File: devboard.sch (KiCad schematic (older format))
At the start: 1 part

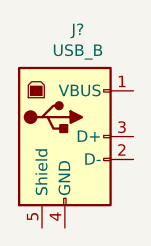
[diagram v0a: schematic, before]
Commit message: changed names
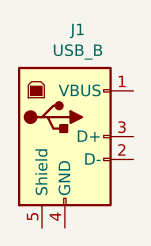
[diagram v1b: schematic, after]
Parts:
- gave numbers to parts that had none: 1
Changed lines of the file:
@@
 encoding utf-8
 Sheet 1 1
-Title "AVR devboard"
-Date "2021-08-16"
-Rev "1.0"
-Comp "Mateusz Wasik Michał Penkal"
+Title "Devboard"
+Date ""
+Rev ""
+Comp ""
 Comment1 ""
 Comment2 ""
@@
 $EndDescr
 $Comp
-L Connector:USB_B J?
+L Connector:USB_B J1
 U 1 1 611B35D4
 P 2500 2950
-F 0 "J?" H 2557 3417 50  0000 C CNN
+F 0 "J1" H 2557 3417 50  0000 C CNN
 F 1 "USB_B" H 2557 3326 50  0000 C CNN
 F 2 "" H 2650 2900 50  0001 C CNN

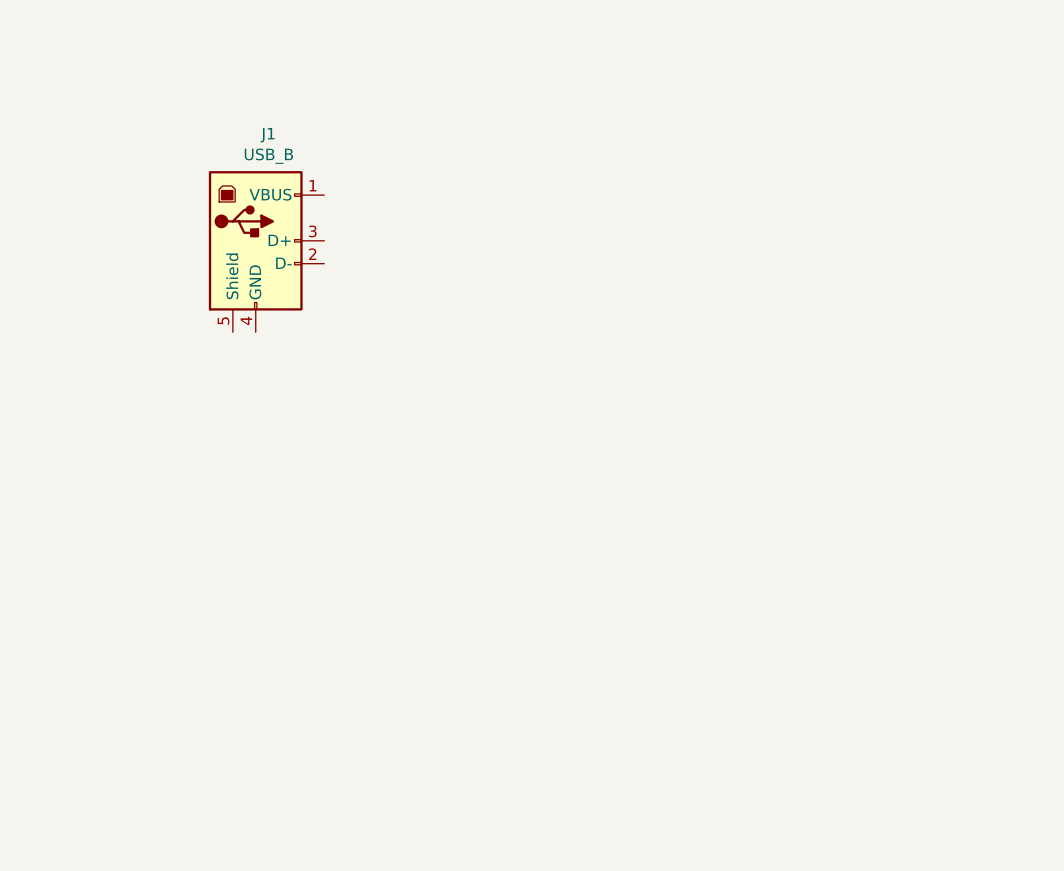
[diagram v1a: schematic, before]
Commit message: Power from USB socket
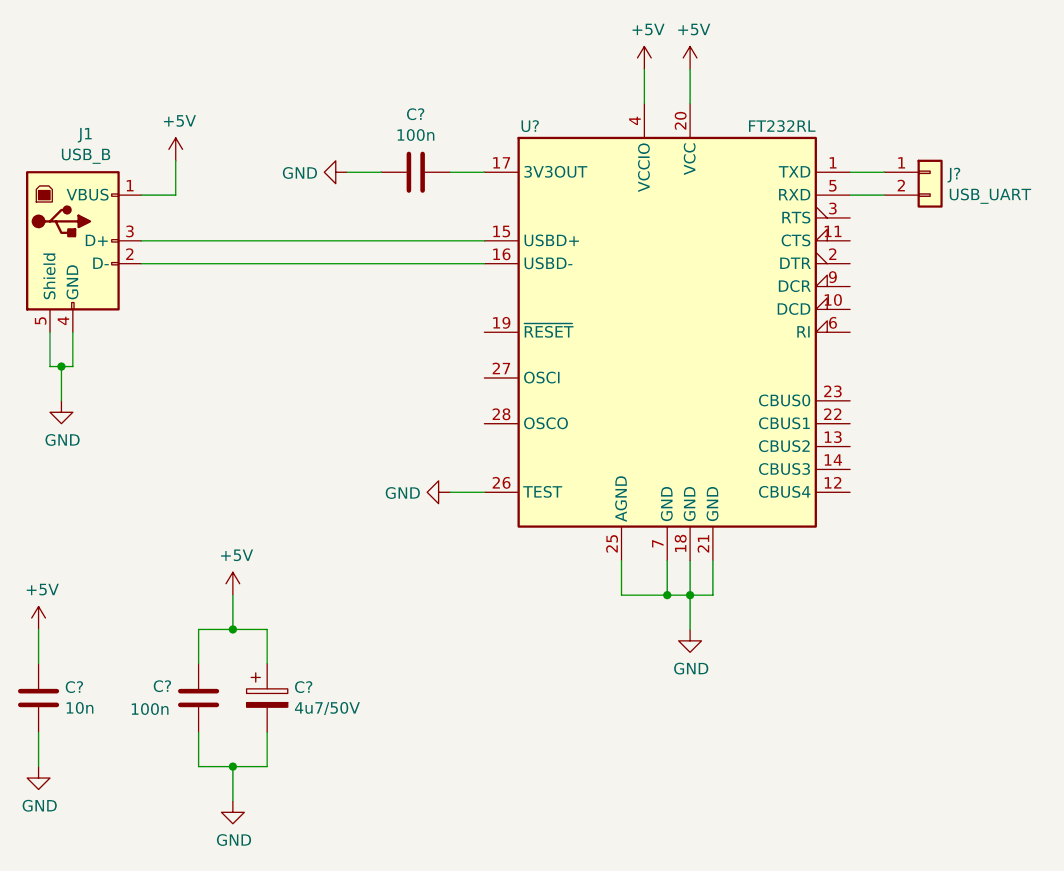
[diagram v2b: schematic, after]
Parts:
- added C? (x2): 100n, symbol Device:C
- added C?: 10n, symbol Device:C
- added C?: 4u7/50V, symbol Device:CP
- added J?: USB_UART, symbol Connector_Generic:Conn_01x02
- added U?: FT232RL, Package_SO:SSOP-28_5.3x10.2mm_P0.65mm, symbol Interface_USB:FT232RL
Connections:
- net +5V: now reaches J1.1 (VBUS)
- net +5V: now also C?.1, C?.2, C?.2, U?.20 (VCC), U?.4 (VCCIO)
- net at J1.2 (D-): now also U?.16 (USBD-)
- net at J1.3 (D+): now also U?.15 (USBD+)
- net GND: now reaches J1.4 (GND)
- net GND: now also J1.5 (Shield), C?.1, C?.1, C?.2, C?.2, U?.18 (GND), U?.21 (GND), U?.25 (AGND), U?.26 (TEST), U?.7 (GND)
- new net: J?.1 (Pin_1), U?.1 (TXD)
- new net: C?.1, U?.17 (3V3OUT)
- new net: J?.2 (Pin_2), U?.5 (RXD)
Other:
- moved on the sheet: J1

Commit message: power dokończony essa
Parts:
- added C?: 10u, symbol Device:CP
- added J?: USB_Control, symbol Connector_Generic:Conn_01x06
- added J?: USB_CBUS, symbol Connector_Generic:Conn_01x06
- added U?: ATmega8A, Package_DIP:DIP-28_W7.62mm, symbol MCU_Microchip_ATmega:ATmega8A-PU
- added Y?: 12M, symbol Device:Crystal_Small
- C?: value 4u7/50V -> 4u7
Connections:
- net +5V: now also C?.1
- net GND: now also C?.2
- net at U?.10 (DCD): now also J?.5 (Pin_5)
- net at U?.11 (CTS): now also J?.2 (Pin_2)
- net at U?.12 (CBUS4): now also J?.5 (Pin_5)
- net at U?.13 (CBUS2): now also J?.3 (Pin_3)
- net at U?.14 (CBUS3): now also J?.4 (Pin_4)
- net at U?.19 (~RESET~): now also J?.6 (Pin_6)
- net at U?.2 (DTR): now also J?.3 (Pin_3)
- net at U?.22 (CBUS1): now also J?.2 (Pin_2)
- net at U?.23 (CBUS0): now also J?.1 (Pin_1)
- net at U?.27 (OSCI): now also Y?.1
- net at U?.28 (OSCO): now also Y?.2
- net at U?.3 (RTS): now also J?.1 (Pin_1)
- net at U?.6 (RI): now also J?.6 (Pin_6)
- net at U?.9 (DCR): now also J?.4 (Pin_4)
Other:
- note added: "USB + Power"
- moved on the sheet: C?, J1, J?, U?

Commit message: MCU + CLK
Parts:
- added C? (x3): 100n, symbol Device:C
- added C?: 10n, symbol Device:C
- added C? (x2): 22p, symbol Device:C
- added JP?: Reset, symbol Device:Jumper_NC_Small
- added JP?: ARef, symbol Device:Jumper_NC_Small
- added JP?: XTAL1, symbol Device:Jumper_NC_Small
- added JP?: XTAL2, symbol Device:Jumper_NC_Small
- added L?: 10u, symbol Device:L
- added R?: 10k, symbol Device:R
- added U?: MCP1525, Package_TO_SOT_THT:TO-92_Inline, symbol Reference_Voltage:MCP1525-TO
- added Y?: 16M, symbol Device:Crystal_Small
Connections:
- net +5V: now also U?.7 (VCC), C?.2, C?.2, L?.1, R?.2, U?.3 (Vin)
- net GND: now also U?.22 (AGND), U?.8 (GND), C?.1, C?.1, C?.1, C?.1, C?.2, C?.2, U?.1 (Vss)
- net Reset: now reaches U?.1 (PC6/~RESET)
- net Reset: now also JP?.2
- net XTAL2: now reaches U?.10 (PB7/XTAL2)
- net XTAL2: now also JP?.2
- net at U?.20 (AVCC): now also C?.2, L?.2
- net A_Ref: now reaches U?.21 (AREF)
- net A_Ref: now also JP?.2
- net XTAL1: now reaches U?.9 (PB6/XTAL1)
- net XTAL1: now also JP?.2
- new net: JP?.1, R?.1
- new net: C?.2, JP?.1, U?.2 (Vout)
- new net: C?.1, JP?.1, Y?.1
- new net: C?.1, JP?.1, Y?.2

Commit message: Programming, port goldpins, a bit of cleanup
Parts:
- added J?: PORTB, symbol Connector_Generic:Conn_01x08
- added J?: PORTC, symbol Connector_Generic:Conn_01x07
- added J?: PORTD, symbol Connector_Generic:Conn_01x08
- added J?: AVR-ISP, symbol Connector:AVR-ISP-10
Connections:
- net +5V: now also J?.2 (VCC)
- net GND: now also J?.10 (GND), J?.4 (GND), J?.6 (GND), J?.8 (GND)
- net PD5: now reaches U?.11 (PD5)
- net PD5: now also J?.6 (Pin_6)
- net PD6: now reaches U?.12 (PD6)
- net PD6: now also J?.7 (Pin_7)
- net PD7: now reaches U?.13 (PD7)
- net PD7: now also J?.8 (Pin_8)
- net PB0: now reaches U?.14 (PB0)
- net PB0: now also J?.1 (Pin_1)
- net PB1: now reaches U?.15 (PB1)
- net PB1: now also J?.2 (Pin_2)
- net PB2: now reaches U?.16 (PB2)
- net PB2: now also J?.3 (Pin_3)
- net MOSI: now reaches U?.17 (PB3)
- net MOSI: now also J?.1 (MOSI), J?.4 (Pin_4)
- net MISO: now reaches U?.18 (PB4)
- net MISO: now also J?.5 (Pin_5), J?.9 (MISO)
- net PB5: now reaches U?.19 (PB5)
- net PB5: now also J?.6 (Pin_6), J?.7 (SCK)
- net PD0: now reaches U?.2 (PD0)
- net PD0: now also J?.1 (Pin_1)
- net PC0: now reaches U?.23 (PC0)
- net PC0: now also J?.1 (Pin_1)
- net PC1: now reaches U?.24 (PC1)
- net PC1: now also J?.2 (Pin_2)
- net PC2: now reaches U?.25 (PC2)
- net PC2: now also J?.3 (Pin_3)
- net PC3: now reaches U?.26 (PC3)
- net PC3: now also J?.4 (Pin_4)
- net PC4: now reaches U?.27 (PC4)
- net PC4: now also J?.5 (Pin_5)
- net PC5: now reaches U?.28 (PC5)
- net PC5: now also J?.6 (Pin_6)
- net PD1: now reaches U?.3 (PD1)
- net PD1: now also J?.2 (Pin_2)
- net PD2: now reaches U?.4 (PD2)
- net PD2: now also J?.3 (Pin_3)
- net PD3: now reaches U?.5 (PD3)
- net PD3: now also J?.4 (Pin_4)
- net PD4: now reaches U?.6 (PD4)
- net PD4: now also J?.5 (Pin_5)
- net Reset renamed PC6
- net PC6: now also J?.5 (~RST), J?.7 (Pin_7)
- net XTAL1 renamed PB6
- net PB6: now also J?.7 (Pin_7)
- net XTAL2 renamed PB7
- net PB7: now also J?.8 (Pin_8)
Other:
- note added: "Crystal"
- note added: "Ports"
- note added: "Prog"
- note added: "Reset"
- note added: "Vref"
- moved on the sheet: C?, J1, J?, JP?, L?, R?, U?, Y?

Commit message: Added relays
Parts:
- added D? (x3): 1N4007, Diode_THT:D_DO-41_SOD81_P10.16mm_Horizontal, symbol Diode:1N4007
- added J?: Relay 1, symbol Connector_Generic:Conn_01x03
- added J?: Relay 1, symbol Connector_Generic:Conn_01x01
- added J?: Relay 2, symbol Connector_Generic:Conn_01x03
- added J?: Relay 2, symbol Connector_Generic:Conn_01x01
- added J?: Relay 3, symbol Connector_Generic:Conn_01x03
- added J?: Relay 3, symbol Connector_Generic:Conn_01x01
- added K1, K2, K?: HF3FA-012-ZTF, symbol hello-there:HF3FA-012-ZTF
- added Q? (x3): BC547, Package_TO_SOT_THT:TO-92_Inline, symbol Transistor_BJT:BC547
- added R? (x3): 1k, symbol Device:R
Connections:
- net +5V: now also D?.1 (K), D?.1 (K), D?.1 (K), K1.1, K2.1, K?.1
- net GND: now also Q?.3 (E), Q?.3 (E), Q?.3 (E)
- new net: D?.2 (A), K1.2, Q?.1 (C)
- new net: Q?.2 (B), R?.1 (x3)
- new net: J?.1 (Pin_1), K1.5
- new net: J?.2 (Pin_2), K1.4
- new net: J?.3 (Pin_3), K1.3
- new net: J?.1 (Pin_1), R?.2 (x3)
- new net: D?.2 (A), K2.2, Q?.1 (C)
- new net: J?.1 (Pin_1), K2.5
- new net: J?.2 (Pin_2), K2.4
- new net: J?.3 (Pin_3), K2.3
- new net: D?.2 (A), K?.2, Q?.1 (C)
- new net: J?.1 (Pin_1), K?.5
- new net: J?.2 (Pin_2), K?.4
- new net: J?.3 (Pin_3), K?.3
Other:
- note added: "Relays"
- moved on the sheet: C?, J1, J?, JP?, L?, R?, U?, Y?

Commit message: LED
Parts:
- added D? (x8): LED, symbol Device:LED
- added J? (x2): Conn_01x08, symbol Connector_Generic:Conn_01x08
- added R? (x8): 75, symbol Device:R
- added SW? (x8): SW_DIP_x01, symbol Switch:SW_DIP_x01
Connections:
- net GND: now also R?.2, R?.2, R?.2, R?.2, R?.2, R?.2, R?.2, R?.2, SW?.2, SW?.2, SW?.2, SW?.2, SW?.2, SW?.2, SW?.2, SW?.2
- new net: D?.1 (K), R?.1 (x8)
- new net: D?.2 (A), J?.2 (Pin_2)
- new net: D?.2 (A), J?.1 (Pin_1)
- new net: D?.2 (A), J?.3 (Pin_3)
- new net: D?.2 (A), J?.4 (Pin_4)
- new net: D?.2 (A), J?.5 (Pin_5)
- new net: D?.2 (A), J?.6 (Pin_6)
- new net: D?.2 (A), J?.7 (Pin_7)
- new net: D?.2 (A), J?.8 (Pin_8)
- new net: J?.1 (Pin_1), SW?.1
- new net: J?.2 (Pin_2), SW?.1
- new net: J?.3 (Pin_3), SW?.1
- new net: J?.4 (Pin_4), SW?.1
- new net: J?.5 (Pin_5), SW?.1
- new net: J?.6 (Pin_6), SW?.1
- new net: J?.7 (Pin_7), SW?.1
- new net: J?.8 (Pin_8), SW?.1
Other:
- note added: "LED"

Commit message: buttons in progress
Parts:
- removed J?: Conn_01x08, symbol Connector_Generic:Conn_01x08
- removed SW? (x8): SW_DIP_x01, symbol Switch:SW_DIP_x01
- added C? (x12): 100n, symbol Device:C
- added J?: DB Buttons, symbol Connector_Generic:Conn_01x04
- added J?: NDB Buttons, symbol Connector_Generic:Conn_01x04
- added R? (x12): 4k7, symbol Device:R
- added R? (x12): 330, symbol Device:R
- added SW?: B1, symbol Switch:SW_Push
- added SW?: B2, symbol Switch:SW_Push
- added SW?: B3, symbol Switch:SW_Push
- added SW?: B4, symbol Switch:SW_Push
- added SW?: B5, symbol Switch:SW_Push
- added SW?: B6, symbol Switch:SW_Push
- added SW?: B7, symbol Switch:SW_Push
- added SW?: B8, symbol Switch:SW_Push
- added SW?: Switches, symbol Switch:SW_DIP_x08
- J?: value Conn_01x08 -> LED
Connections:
- net +5V: now also R?.1, R?.1, R?.1, R?.1, R?.1, R?.1, R?.1, R?.1, R?.1, R?.1, R?.1, R?.1
- net GND: now also C?.2, C?.2, C?.2, C?.2, C?.2, C?.2, C?.2, C?.2, C?.2, C?.2, C?.2, C?.2, R?.2, R?.2, R?.2, R?.2, SW?.10, SW?.11, SW?.12, SW?.13, SW?.14, SW?.15, SW?.16, SW?.2, SW?.2, SW?.2, SW?.2, SW?.9
- new net: R?.1, SW?.2 (x4)
- new net: R?.2, SW?.1
- new net: R?.2, SW?.2
- new net: R?.2, SW?.3
- new net: R?.2, SW?.4
- new net: R?.2, SW?.5
- new net: R?.2, SW?.6
- new net: R?.2, SW?.7
- new net: R?.2, SW?.8
- new net B1: C?.1, J?.1 (Pin_1), R?.2, SW?.1
- new net B2: C?.1, J?.2 (Pin_2), R?.2, SW?.1
- new net B3: C?.1, J?.3 (Pin_3), R?.2, SW?.1
- new net B4: C?.1, J?.4 (Pin_4), R?.2, SW?.1
- new net B5: J?.1 (Pin_1), SW?.1
- new net B6: J?.2 (Pin_2), SW?.1
- new net B7: J?.3 (Pin_3), SW?.1
- new net B8: J?.4 (Pin_4), SW?.1
- new net S1: C?.1, R?.1, R?.2
- new net S2: C?.1, R?.1, R?.2
- new net S3: C?.1, R?.1, R?.2
- new net S4: C?.1, R?.1, R?.2
- new net S5: C?.1, R?.1, R?.2
- new net S6: C?.1, R?.1, R?.2
- new net S7: C?.1, R?.1, R?.2
- new net S8: C?.1, R?.1, R?.2
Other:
- note added: "CPU"
- note added: "Debounced buttons"
- note added: "Non-debounced buttons"
- moved on the sheet: C?, D?, J?, L?, R?, U?
